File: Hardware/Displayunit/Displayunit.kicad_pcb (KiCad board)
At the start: 4 copper layers, 155 x 64.8 mm, 142 parts, among them IC1 TSC2007, IC2 MX25LM51245GXDI00, IC3 IS66WVH8M8BLL-100B1LI_0, IC4 TPS61165DRVR, J1 615008138221, J10 ER-CON10HT-1, J2 615008138221, J3 54104-4031, J4 Conn_ARM_JTAG_SWD_20, J5 52271-0679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

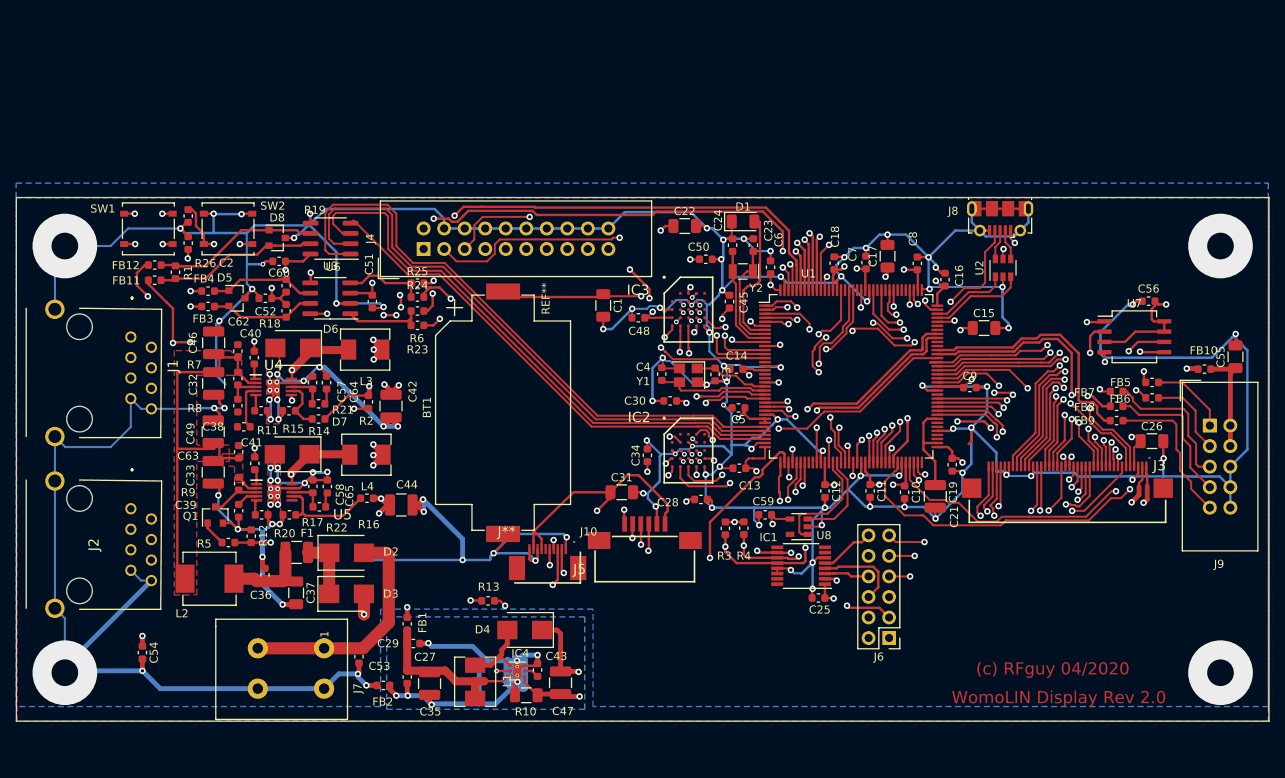
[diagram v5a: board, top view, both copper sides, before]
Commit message: lengthmatch octospi on flash and ram
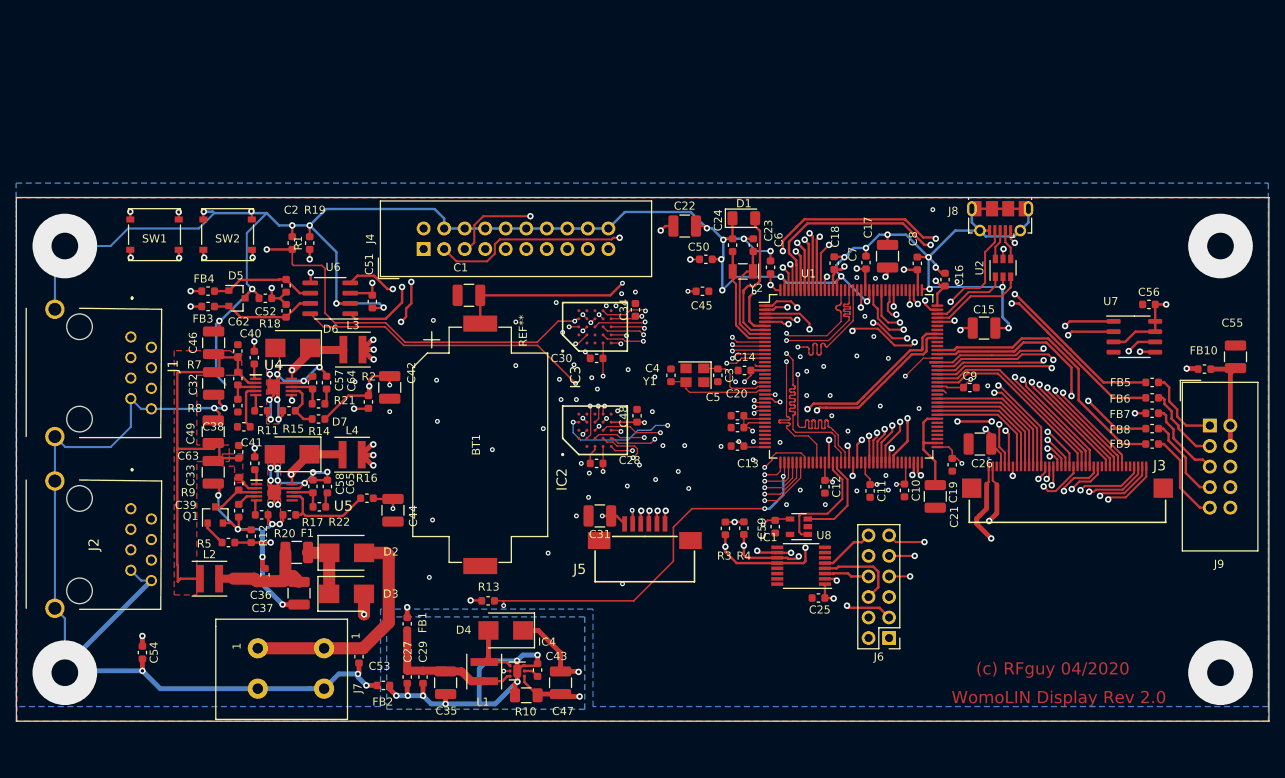
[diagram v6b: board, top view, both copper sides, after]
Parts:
- removed C60: 100n, Capacitor_SMD:C_0603_1608Metric
- removed D8: NUP2105L, Package_TO_SOT_SMD:SOT-23
- removed FB11, FB12: 100R, Inductor_SMD:L_0603_1608Metric
- removed J10: ER-CON10HT-1, Womo-Lin:ER-CON10HT-1
- removed R23, R24, R25, R6: 0R, Resistor_SMD:R_0603_1608Metric
- removed R26: 120R, Resistor_SMD:R_0603_1608Metric
- removed U3: HD588E, Package_SO:SOIC-8_3.9x4.9mm_P1.27mm
- added C20: 100n, Capacitor_SMD:C_0603_1608Metric, F.Cu at (151.2, 77.5)
- C1, C15, C17, C22, C26, C31, C37, C55: footprint Capacitor_SMD:C_1206_3216Metric -> Capacitor_SMD:C_1210_3225Metric
- FB5, FB6, FB7, FB8, FB9: value 100r -> BLM18PG121SN1D
- IC4: footprint Package_SON:WSON-6-1EP_2x2mm_P0.65mm_EP1x1.6mm_ThermalVias -> Package_SON:WSON-6-1EP_2x2mm_P0.65mm_EP1x1.6mm
- L1, L3, L4: footprint Womo-Lin:MWSA0503 -> Inductor_SMD:L_Coilcraft_XxL4020
- L2: footprint Womo-Lin:MWSA0603 -> Inductor_SMD:L_Coilcraft_XxL4020
- R1, R13, R15, R2, R3, R4: value 10k -> 10K
- R14: value 31k6 -> 31K6
- U7: footprint Package_SO:SO-8_5.3x6.2mm_P1.27mm -> Package_SO:SO-8_3.9x4.9mm_P1.27mm
- moved C26 21.3 mm to (181.2, 79.5), turned to 180 degrees
- moved C34 18.1 mm to (138.6, 62.9)
- moved C1 16.7 mm to (118.0, 61.1), turned to 180 degrees
- moved R1 15.0 mm to (98.3, 54.6)
- moved C28 13.7 mm to (133.8, 81.9), turned to 180 degrees
- moved C2 13.3 mm to (96.1, 54.6), turned to 90 degrees
- moved C48 12.1 mm to (138.8, 76.0), turned to 90 degrees
- moved IC2 11.8 mm to (133.6, 77.8), turned to 90 degrees
- moved IC3 11.8 mm to (133.6, 65.0), turned to 90 degrees
- moved C30 10.5 mm to (133.8, 68.9)
- moved FB9 5.26 mm to (202.5, 79.5)
- moved FB8 5.19 mm to (202.5, 77.6)
- moved FB7 5.15 mm to (202.5, 75.7)
- moved BT1 4.87 mm to (119.4, 79.6)
- moved C29 4.31 mm to (112.3, 108.3), turned to 270 degrees
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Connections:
- J1 pad 3: Net-(FB12-Pad1) -> Net-(J1-Pad3)
- J1 pad 6: Net-(FB11-Pad1) -> Net-(J1-Pad6)
- J2 pad 3: Net-(FB12-Pad1) -> Net-(J2-Pad3)
- J2 pad 6: Net-(FB11-Pad1) -> Net-(J2-Pad6)
- U1 pad 139: CAN1_RX -> EXT_1
- U1 pad 140: CAN1_TX -> EXT_2
- U1 pad 31: USART2_CTS_NSS -> Net-(U1-Pad31)
- U1 pad 32: USART2_RTS_DE -> Net-(U1-Pad32)
- U1 pad 33: USART2_TX -> Net-(U1-Pad33)
- U1 pad 34: USART2_RX -> Net-(U1-Pad34)
- U1 pad 65: EXT_1 -> EXT_3
- U1 pad 66: EXT_2 -> Net-(U1-Pad66)
- U1 pad 69: EXT_3 -> Net-(U1-Pad69)
- U6 pad 1: Net-(R23-Pad1) -> USART1_TX
- U6 pad 4: Net-(R24-Pad1) -> USART1_RX
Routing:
- net GND: track 922.7 -> 498.3 mm, vias 119 -> 126
- net +3V3: track 410.6 -> 222.4 mm, vias 40 -> 35
- net USART2_CTS_NSS: track 77.3 -> 0.00 mm
- net USART2_RTS_DE: track 74.0 -> 0.00 mm
- net USART2_TX: track 71.0 -> 0.00 mm
- net +3.3VA: track 182.9 -> 118.3 mm, vias 11 -> 10
- net CAN1_TX: track 64.4 -> 0.00 mm, vias 2 -> 0
- net CAN1_RX: track 63.4 -> 0.00 mm, vias 4 -> 0
- net USART2_RX: track 62.6 -> 0.00 mm
- net Net-(FB11-Pad1): track 47.1 -> 0.00 mm, vias 2 -> 0
- net OctoSPI_P2_IO0: track 12.8 -> 50.6 mm
- net Net-(FB12-Pad1): track 36.2 -> 0.00 mm, vias 1 -> 0
- net OctoSPI_P2_IO2: track 12.1 -> 45.1 mm
- net OctoSPI_P2_IO3: track 12.9 -> 45.0 mm
- net OctoSPI_P1_IO3: track 16.3 -> 47.0 mm, vias 2 -> 3
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- added copper zone on In1.Cu, net GND
- added copper zone on B.Cu, net LCD_LED-K
- removed copper zone on B.Cu, net Net-(C27-Pad2)
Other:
- rule trace_min: 0.2 -> 0.15
- board text added: "sync was here"

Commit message: Display Unit Zusätzliche Buchsen Mini Fit für den Bus, Befestigung um 5mm verschoben, Bauteil Placement.
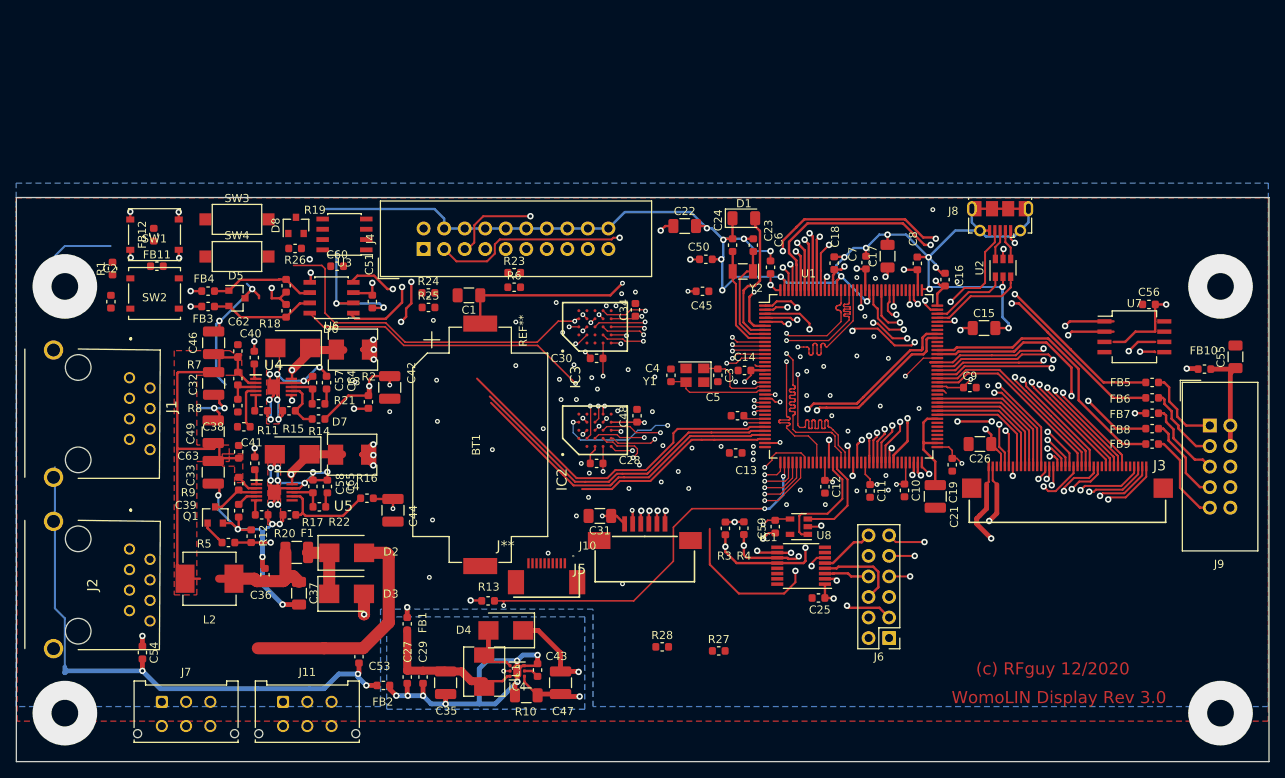
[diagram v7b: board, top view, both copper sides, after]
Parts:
- removed C20: 100n, Capacitor_SMD:C_0603_1608Metric
- removed C52: 5n6, Capacitor_SMD:C_0603_1608Metric
- added C60: 100n, Capacitor_SMD:C_0603_1608Metric, F.Cu at (101.7, 57.5)
- added D8: NUP2105L, Package_TO_SOT_SMD:SOT-23, F.Cu at (96.6, 52.5)
- added FB11: 100R, Inductor_SMD:L_0603_1608Metric, F.Cu at (79.4, 57.5)
- added FB12: 100R, Inductor_SMD:L_0603_1608Metric, F.Cu at (79.0, 53.6)
- added J10: ER-CON10HT-1, Womo-Lin:ER-CON10HT-1, F.Cu at (127.6, 97.2)
- added J11: Conn_02x03_Row_Letter_First, Connector_Molex:Molex_Micro-Fit_3.0_43045-0612_2x03_P3.00mm_Vertical, F.Cu at (95.0, 111.4)
- added R23: 0R, Resistor_SMD:R_0603_1608Metric, F.Cu at (123.6, 58.3)
- added R24: 0R, Resistor_SMD:R_0603_1608Metric, F.Cu at (113.0, 60.8)
- added R25: 0R, Resistor_SMD:R_0603_1608Metric, F.Cu at (113.0, 62.6)
- added R26: 120R, Resistor_SMD:R_0603_1608Metric, F.Cu at (96.5, 55.3)
- added R27: 4k7, Resistor_SMD:R_0603_1608Metric, F.Cu at (148.9, 105.1)
- added R28: 4k7, Resistor_SMD:R_0603_1608Metric, F.Cu at (141.9, 104.6)
- added R6: 0R, Resistor_SMD:R_0603_1608Metric, F.Cu at (123.6, 60.1)
- added SW3: SW_DIP_x01, Button_Switch_SMD:SW_SPST_CK_RS282G05A3, F.Cu at (89.3, 51.7)
- added SW4: SW_DIP_x01, Button_Switch_SMD:SW_SPST_CK_RS282G05A3, F.Cu at (89.3, 56.3)
- added U3: HD588E, Package_SO:SOIC-8_3.9x4.9mm_P1.27mm, F.Cu at (102.6, 53.6)
- C1, C15, C22, C31, C37, C55: footprint Capacitor_SMD:C_1210_3225Metric -> Capacitor_SMD:C_1206_3216Metric
- C17: value 10uF -> 10u; footprint Capacitor_SMD:C_1210_3225Metric -> Capacitor_SMD:C_1206_3216Metric
- C26: value 1uF -> 1u; footprint Capacitor_SMD:C_1210_3225Metric -> Capacitor_SMD:C_1206_3216Metric
- C42: value 22uF -> 22u
- C44: value 47u -> 22u
- FB5, FB6, FB7, FB8, FB9: value BLM18PG121SN1D -> 100r
- IC4: footprint Package_SON:WSON-6-1EP_2x2mm_P0.65mm_EP1x1.6mm -> Package_SON:WSON-6-1EP_2x2mm_P0.65mm_EP1x1.6mm_ThermalVias
- J7: value WAGO_Klemmleiste_2-pol -> Conn_02x03_Row_Letter_First; footprint WAGO:WAGO_Klemmleiste_Hebel4mm²Horizontal_RM5mm_2-pol -> Connector_Molex:Molex_Micro-Fit_3.0_43045-0612_2x03_P3.00mm_Vertical
- L1, L3, L4: footprint Inductor_SMD:L_Coilcraft_XxL4020 -> Womo-Lin:MWSA0503
- L2: footprint Inductor_SMD:L_Coilcraft_XxL4020 -> Womo-Lin:MWSA0603
- R1, R13, R15, R2, R3, R4: value 10K -> 10k
- R14: value 31K6 -> 31k6
- R18: value 60R -> 120R
- U6: value SN65HVD231DR -> SN65HVD234
- U7: footprint Package_SO:SO-8_3.9x4.9mm_P1.27mm -> Package_SO:SO-8_5.3x6.2mm_P1.27mm
- moved R1 24.6 mm to (73.9, 57.8)
- moved C2 23.6 mm to (73.7, 61.9)
- moved J7 21.1 mm to (80.0, 111.4), turned to 0 degrees
- moved SW2 11.6 mm to (79.1, 60.9)
- moved J1 5.04 mm to (76.0, 71.3)
- moved J2 4.99 mm to (76.0, 92.5)
- moved C13 0.87 mm to (151.0, 80.6)
- moved U6 0.18 mm to (101.0, 61.4)
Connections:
- C53 pad 1: Net-(C53-Pad1) -> Control+2
- D2 pad 2: Net-(C53-Pad1) -> Control+2
- J1 pad 3: Net-(J1-Pad3) -> Net-(FB12-Pad1)
- J1 pad 6: Net-(J1-Pad6) -> Net-(FB11-Pad1)
- J2 pad 3: Net-(J2-Pad3) -> Net-(FB12-Pad1)
- J2 pad 6: Net-(J2-Pad6) -> Net-(FB11-Pad1)
- J7 pad 1: Net-(C53-Pad1) -> (no net)
- J7 pad 2: GND -> (no net)
- R18 pad 2: VrefCAN -> Net-(R18-Pad2)
- R19 pad 1: VrefCAN -> Net-(R19-Pad1)
- R19 pad 2: Net-(D5-Pad1) -> Net-(R19-Pad2)
- U1 pad 139: EXT_1 -> CAN1_RX
- U1 pad 140: EXT_2 -> CAN1_TX
- U1 pad 31: Net-(U1-Pad31) -> USART2_CTS_NSS
- U1 pad 32: Net-(U1-Pad32) -> USART2_RTS_DE
- U1 pad 33: Net-(U1-Pad33) -> USART2_TX
- U1 pad 34: Net-(U1-Pad34) -> USART2_RX
- U1 pad 65: EXT_3 -> EXT_1
- U1 pad 66: Net-(U1-Pad66) -> EXT_2
- U1 pad 69: Net-(U1-Pad69) -> EXT_3
- U1 pad 72: Net-(U1-Pad72) -> CAN_EN
- U6 pad 1: USART1_TX -> Net-(R23-Pad1)
- U6 pad 4: USART1_RX -> Net-(R24-Pad1)
- U6 pad 5: VrefCAN -> CAN_EN
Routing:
- net GND: track 498.3 -> 410.0 mm, vias 126 -> 125
- net Control+: track 82.5 -> 5.25 mm
- net USART2_CTS_NSS: track 0.00 -> 44.1 mm
- net CAN_EN: track 0.00 -> 43.1 mm, vias 0 -> 2
- net USART2_RTS_DE: track 0.00 -> 41.0 mm
- net USART2_TX: track 0.00 -> 40.7 mm
- net Net-(C53-Pad1): track 29.6 -> 0.00 mm
- net Control+2: track 0.00 -> 29.6 mm
- net USART2_RX: track 0.00 -> 25.2 mm
- net Net-(FB4-Pad1): track 42.2 -> 17.4 mm
- net Net-(FB3-Pad1): track 34.6 -> 10.3 mm
- net RESET: track 108.1 -> 91.6 mm, vias 7 -> 4
- net Boot0: track 102.6 -> 95.4 mm
- net +3V3: track 222.4 -> 215.3 mm
- net I2C2_SDA: track 62.6 -> 58.8 mm
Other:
- board size 155 x 64.8 mm -> 155 x 69.8 mm
- board text added: "(c) RFguy 12/2020"
- board text added: "WomoLIN Display Rev 3.0"
- board text removed: "(c) RFguy 04/2020"
- board text removed: "WomoLIN Display Rev 2.0"

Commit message: Fehlende Teile gerouted
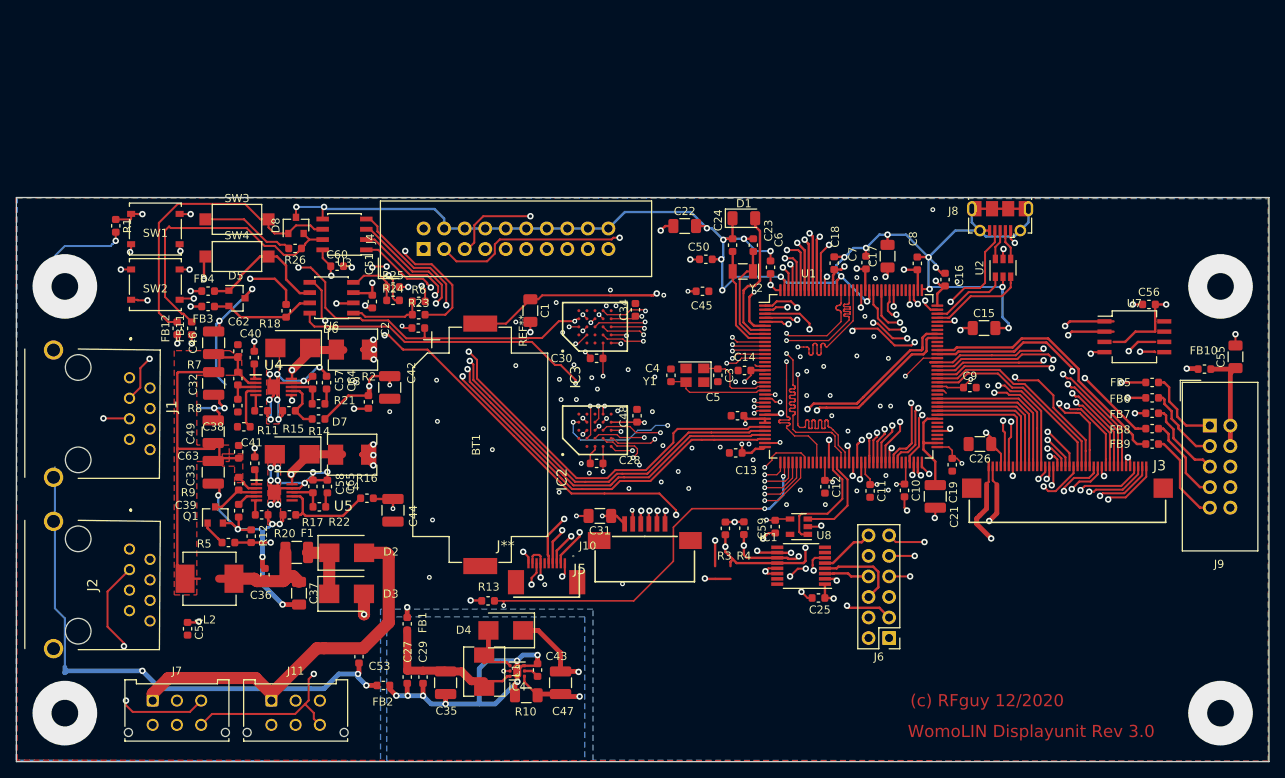
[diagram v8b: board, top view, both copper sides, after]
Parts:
- removed R19: 60R, Resistor_SMD:R_0603_1608Metric
- removed R27, R28: 4k7, Resistor_SMD:R_0603_1608Metric
- J11, J7: value Conn_02x03_Row_Letter_First -> Conn_02x03_Odd_Even
- moved C2 38.2 mm to (111.7, 65.2), turned to 180 degrees
- moved R23 12.9 mm to (111.8, 63.5)
- moved FB12 11.9 mm to (81.9, 65.2)
- moved R6 11.9 mm to (111.8, 61.8)
- moved FB11 8.81 mm to (83.7, 65.2), turned to 90 degrees
- moved C1 7.83 mm to (125.6, 63.0), turned to 270 degrees
- moved C54 6.32 mm to (83.2, 102.4)
- moved R1 5.30 mm to (74.3, 52.5), turned to 270 degrees
- moved R25 5.07 mm to (108.6, 60.1)
- moved R24 4.47 mm to (108.6, 61.7)
- moved J11 1.45 mm to (93.6, 111.3)
- moved J7 1.14 mm to (78.9, 111.3)
- moved SW2 1.10 mm to (79.2, 59.8)
- moved SW1 0.70 mm to (79.2, 52.9)
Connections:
- C25 pad 2: +3.3VA -> +3V3
- C31 pad 1: +3.3VA -> +3V3
- IC1 pad 1: +3.3VA -> +3V3
- J10 pad 7: +3.3VA -> +3V3
- J10 pad 9: +3.3VA -> +3V3
- J11 pad 1: (no net) -> Control+2
- J11 pad 2: (no net) -> Net-(FB3-Pad1)
- J11 pad 3: (no net) -> Net-(FB12-Pad1)
- J11 pad 4: (no net) -> GND
- J11 pad 5: (no net) -> Net-(FB4-Pad1)
- J11 pad 6: (no net) -> Net-(FB11-Pad1)
- J5 pad 1: +3.3VA -> +3V3
- J7 pad 1: (no net) -> Control+2
- J7 pad 2: (no net) -> Net-(FB3-Pad1)
- J7 pad 3: (no net) -> Net-(FB12-Pad1)
- J7 pad 4: (no net) -> GND
- J7 pad 5: (no net) -> Net-(FB4-Pad1)
- J7 pad 6: (no net) -> Net-(FB11-Pad1)
- R3 pad 1: +3.3VA -> +3V3
- R4 pad 1: +3.3VA -> +3V3
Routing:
- net Net-(FB11-Pad1): track 0.00 -> 83.8 mm, vias 0 -> 2
- net Net-(FB12-Pad1): track 0.00 -> 80.4 mm, vias 0 -> 4
- net Net-(FB4-Pad1): track 17.4 -> 95.8 mm, vias 1 -> 2
- net +3.3VA: track 118.3 -> 40.5 mm, vias 10 -> 8
- net Net-(FB3-Pad1): track 10.3 -> 76.4 mm
- net Control+: track 5.25 -> 69.5 mm
- net CAN_EN: track 43.1 -> 102.7 mm, vias 2 -> 6
- net CAN1_RX: track 0.00 -> 56.4 mm, vias 0 -> 2
- net CAN1_TX: track 0.00 -> 53.6 mm, vias 0 -> 2
- net USART2_RX: track 25.2 -> 72.2 mm, vias 0 -> 2
- net Net-(D8-Pad1): track 0.00 -> 37.9 mm
- net Net-(D8-Pad2): track 0.00 -> 35.9 mm
- net USART2_TX: track 40.7 -> 72.4 mm, vias 0 -> 2
- net USART2_RTS_DE: track 41.0 -> 70.1 mm, vias 0 -> 2
- net GND: track 410.0 -> 438.6 mm, vias 125 -> 147
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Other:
- board text added: "WomoLIN Displayunit Rev 3.0"
- board text removed: "WomoLIN Display Rev 3.0"
